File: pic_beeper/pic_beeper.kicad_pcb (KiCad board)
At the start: 2 copper layers, 33 x 26.7 mm, 7 parts, among them J1 Conn_01x06, SW1 SW_SPDT, U1 PIC12F752-IP

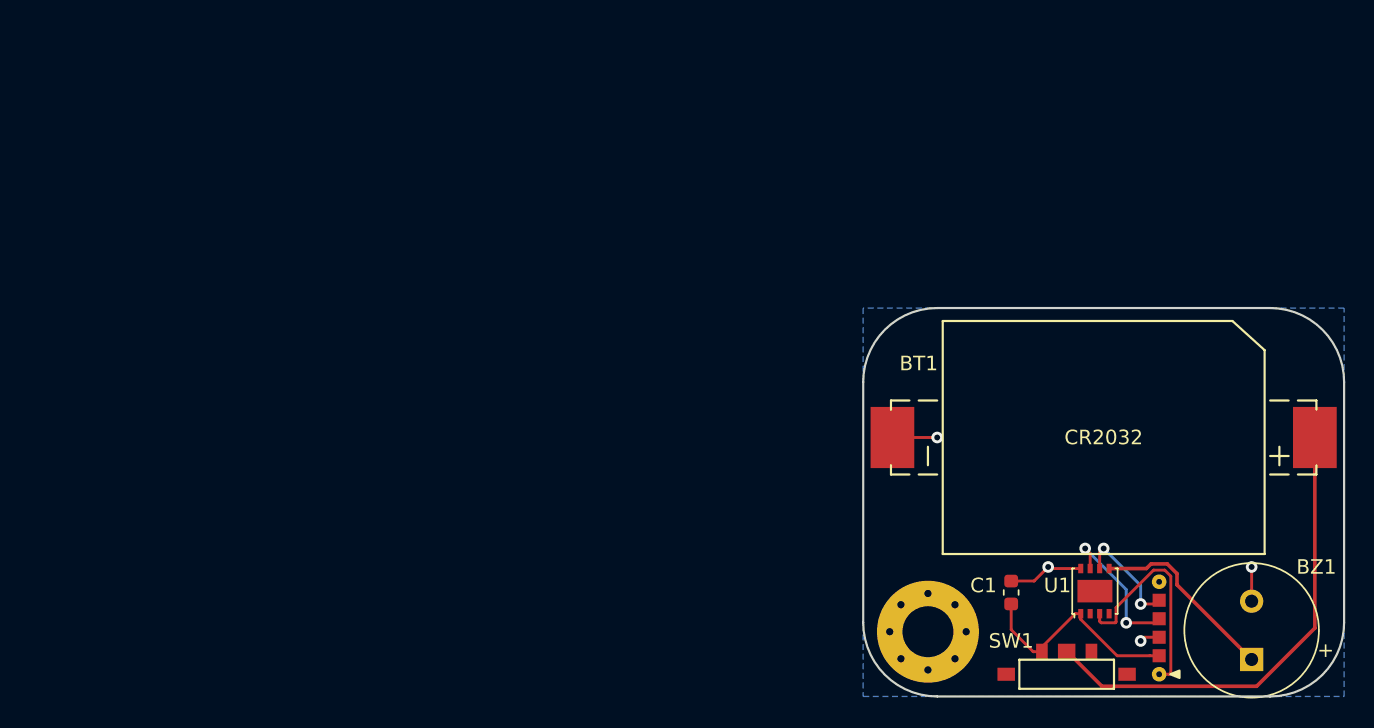
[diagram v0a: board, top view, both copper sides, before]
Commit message: Stop using temp sense osc
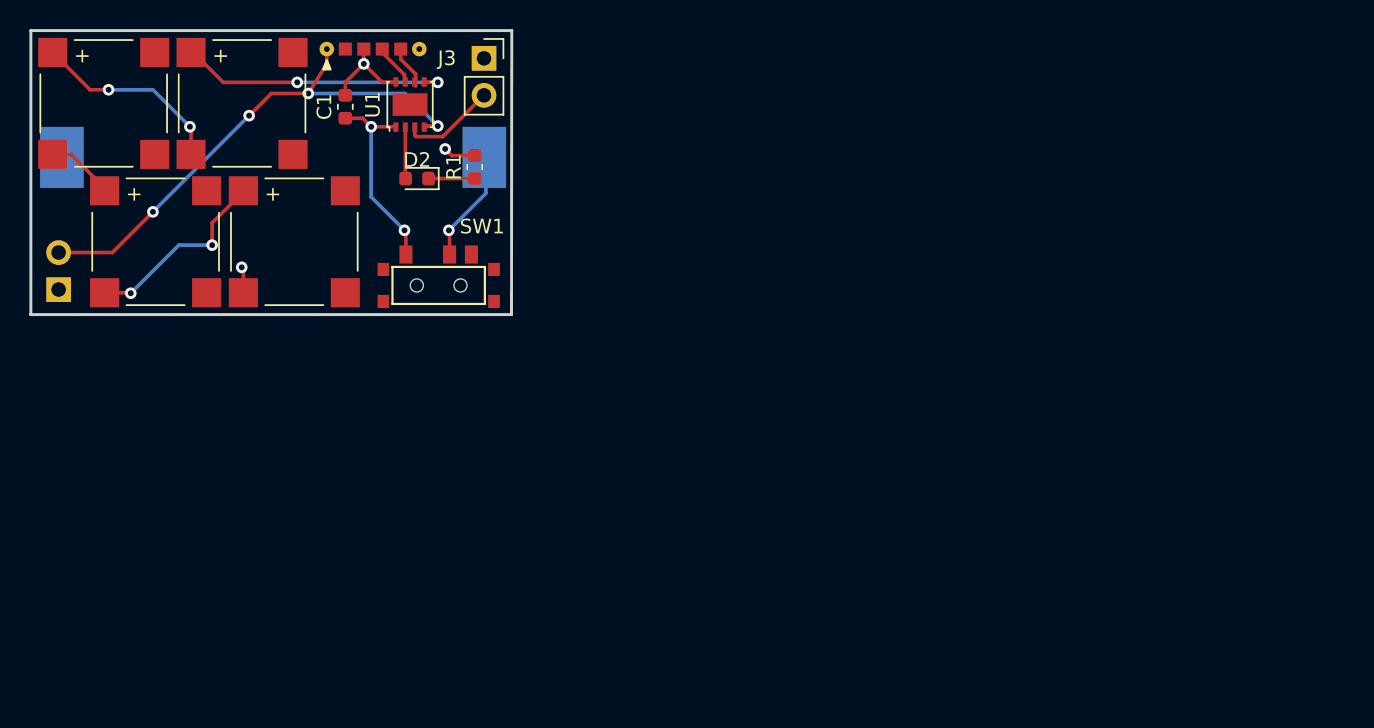
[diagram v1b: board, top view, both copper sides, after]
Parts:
- removed H1: MountingHole_Pad, MountingHole:MountingHole_3.5mm_Pad_Via
- added BZ2: 16R, Buzzer_Beeper:PUIAudio_SMT_0825_S_4_R, F.Cu at (5.00, 5.00)
- added BZ3: 16R, Buzzer_Beeper:PUIAudio_SMT_0825_S_4_R, F.Cu at (8.56, 14.5)
- added BZ4: 16R, Buzzer_Beeper:PUIAudio_SMT_0825_S_4_R, F.Cu at (18.1, 14.5)
- added D2: LED, LED_SMD:LED_0603_1608Metric, F.Cu at (26.5, 10.2)
- added J2: Conn_01x02_Male, Connector_PinHeader_2.54mm:PinHeader_1x02_P2.54mm_Vertical, B.Cu at (1.91, 17.8)
- added J3: Conn_01x02_Female, Connector_PinSocket_2.54mm:PinSocket_1x02_P2.54mm_Vertical, F.Cu at (31.1, 1.91)
- added R1: 140R, Resistor_SMD:R_0603_1608Metric, F.Cu at (30.5, 9.37)
- BT1: moved to B.Cu
- BZ1: value Buzzer -> 16R; footprint Buzzer_Beeper:MagneticBuzzer_CUI_CST-931RP-A -> Buzzer_Beeper:PUIAudio_SMT_0825_S_4_R
- SW1: footprint lib_fp:SW_SPDT_SSAL220100 -> lib_fp:SW_SPDT_SK3296
- U1: value PIC12F752-IP -> PIC12F752
- moved BZ1 79.1 mm to (14.5, 5.00), turned to 0 degrees
- moved J1 66.5 mm to (23.9, 1.27), turned to 0 degrees
- moved BT1 60.2 mm to (16.6, 8.71)
- moved U1 57.7 mm to (26.0, 5.08)
- moved C1 56.6 mm to (21.6, 5.23)
- moved SW1 50.7 mm to (28.0, 17.5), turned to 180 degrees
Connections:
- BZ1 pad 2: -BATT -> Net-(BZ1-Pad2)
- U1 pad 3: /VPP -> /SLAVE_RESET
- U1 pad 4: Net-(U1-Pad4) -> /VPP
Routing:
- net Net-(BT1-Pad1): track 32.8 -> 7.56 mm, vias 0 -> 1
- net /VPP: track 15.2 -> 35.7 mm, vias 0 -> 4
- net Net-(BZ1-Pad2): track 0.00 -> 13.4 mm, vias 0 -> 2
- net Net-(BZ3-Pad2): track 0.00 -> 13.2 mm, vias 0 -> 2
- net /ICSPDAT: track 10.2 -> 2.92 mm, vias 2 -> 0
- net /SLAVE_RESET: track 0.00 -> 6.71 mm
- net /BUZZER: track 13.1 -> 18.5 mm, vias 0 -> 2
- net /ICSPCLK: track 7.73 -> 2.96 mm, vias 2 -> 0
- net Net-(BZ2-Pad2): track 0.00 -> 4.53 mm
- net Net-(D2-Pad2): track 0.00 -> 3.47 mm
- net Net-(D2-Pad1): track 0.00 -> 3.18 mm
- net +BATT: track 15.2 -> 13.3 mm, vias 0 -> 2
- net -BATT: track 12.0 -> 10.4 mm, vias 4 -> 3
- added copper zone on F.Cu, net +BATT
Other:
- board size 33 x 26.7 mm -> 33 x 19.5 mm
- board text added: "v2.1"
- board text removed: "BEEP BEEP awyea"
- board text removed: "PIC Beeper v1.0 John McNelly"

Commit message: Make hardware v2.0
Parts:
- removed BT1: CR2032, lib_fp:BatteryHolder_Q&J-CR2032-BS-6-1
- removed BZ2, BZ3, BZ4: 16R, Buzzer_Beeper:PUIAudio_SMT_0825_S_4_R
- added D1: 40V 5A, Diode_SMD:D_SMA, F.Cu at (20.4, 22.9)
- added G***: LOGO, lib_fp:bird_with_pants_small_flipped, B.Cu at (20.2, 18.4)
- added G***: LOGO, lib_fp:bird_with_pants_small, B.Cu at (24.0, 18.4)
- added J4: Conn_01x03_Female, Connector_PinSocket_2.54mm:PinSocket_1x03_P2.54mm_Vertical, B.Cu at (46.4, 23.5)
- added JP1: Open Jumper, Jumper:SolderJumper-2_P1.3mm_Open_Pad1.0x1.5mm, F.Cu at (32.0, 23.9)
- added Q1: BSS138, Package_TO_SOT_SMD:SOT-23, F.Cu at (26.0, 22.9)
- added R2: 10k, Resistor_SMD:R_0603_1608Metric, F.Cu at (35.6, 13.5)
- added R3: DNP, Resistor_SMD:R_0603_1608Metric, F.Cu at (35.6, 16.7)
- J1: moved to B.Cu
- J2: value Conn_01x02_Male -> JST_PH_01x02_Male_RightAngle; footprint Connector_PinHeader_2.54mm:PinHeader_1x02_P2.54mm_Vertical -> Connector_JST:JST_PH_S2B-PH-K_1x02_P2.00mm_Horizontal; moved to F.Cu
- J3: value Conn_01x02_Female -> Conn_01x03_Male; footprint Connector_PinSocket_2.54mm:PinSocket_1x02_P2.54mm_Vertical -> Connector_PinHeader_2.54mm:PinHeader_1x03_P2.54mm_Vertical
- R1: value 140R -> 680R
- moved J2 40.0 mm to (41.9, 17.8), turned to 180 degrees
- moved J3 20.1 mm to (14.5, 13.2)
- moved C1 16.0 mm to (28.4, 19.7), turned to 0 degrees
- moved SW1 13.3 mm to (39.6, 23.9)
- moved BZ1 13.1 mm to (21.3, 16.2), turned to 90 degrees
- moved J1 12.6 mm to (30.2, 12.2), turned to 180 degrees
- moved U1 11.3 mm to (29.2, 15.9), turned to 270 degrees
- moved R1 6.78 mm to (32.4, 15.9), turned to 270 degrees
- moved D2 3.97 mm to (30.0, 12.1)
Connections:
- BZ1 pad 1: /BUZZER -> +BATT
- J1 pad 6: Net-(J1-Pad6) -> (no net)
- J2 pad 1: -BATT -> /BATT_SWITCH
- J2 pad 2: /VPP -> -BATT
- J3 pad 1: -BATT -> /BATT_SWITCH
- J3 pad 2: /SLAVE_RESET -> /VPP
- SW1 pad 2: Net-(BT1-Pad1) -> /BATT_SWITCH
- SW1 pad 3: Net-(SW1-Pad3) -> (no net)
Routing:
- net /BATT_SWITCH: track 0.00 -> 40.0 mm, vias 0 -> 3
- net /SLAVE_RESET: track 6.71 -> 29.1 mm, vias 0 -> 3
- net Net-(BZ3-Pad2): track 13.2 -> 0.00 mm, vias 2 -> 0
- net /BUZZER: track 18.5 -> 8.69 mm
- net Net-(BT1-Pad1): track 7.56 -> 0.00 mm, vias 1 -> 0
- net +BATT: track 13.3 -> 7.38 mm, vias 2 -> 1
- net Net-(BZ1-Pad2): track 13.4 -> 8.39 mm, vias 2 -> 0
- net /ICSPDAT: track 2.92 -> 7.65 mm, vias 0 -> 1
- net /ICSPCLK: track 2.96 -> 7.54 mm, vias 0 -> 1
- net Net-(BZ2-Pad2): track 4.53 -> 0.00 mm
- net -BATT: track 10.4 -> 6.18 mm, vias 3 -> 5
- net /VPP: track 35.7 -> 37.4 mm, vias 4 -> 5
- net Net-(D2-Pad2): track 3.47 -> 2.39 mm
- net Net-(D2-Pad1): track 3.18 -> 3.69 mm
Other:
- board size 33 x 19.5 mm -> 35.6 x 15.2 mm
- board text added: "Pic Beeper v2.0 For my favorite human."
- board text removed: "v2.1"

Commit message: Dump leftovers
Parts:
- moved G*** 6.39 mm to (17.9, 20.3), turned to 180 degrees
- moved G*** 2.44 mm to (21.7, 20.3), turned to 180 degrees
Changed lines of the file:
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@@
   )
   (setup
-    (last_trace_width 0.8)
+    (last_trace_width 0.25)
     (user_trace_width 0.2)
     (user_trace_width 0.25)
@@
   )
   (module lib_fp:bird_with_pants_small_flipped (layer B.Cu)
-    (at 20.193 18.415)
+    (at 21.717 20.32 180)
     (fp_text reference G*** (at 0 0) (layer B.SilkS) hide
       (effects (font (size 1.524 1.524) (thickness 0.3)) (justify mirror))
@@
   )
   (module lib_fp:bird_with_pants_small (layer B.Cu)
-    (at 24.003 18.415)
+    (at 17.907 20.32 180)
     (fp_text reference G*** (at 0 0) (layer B.SilkS) hide
       (effects (font (size 1.524 1.524) (thickness 0.3)) (justify mirror))
@@
     )
   )
-  (gr_poly (pts (xy 22.098 20.32) (xy 21.59 21.082) (xy 21.59 21.336) (xy 21.717 21.463) (xy 21.971 21.463) (xy 22.098 21.336) (xy 22.098 21.209) (xy 22.098 21.336) (xy 22.225 21.463) (xy 22.352 21.463) (xy 22.479 21.463) (xy 22.606 21.336) (xy 22.606 21.082)) (layer B.SilkS) (width 0.1))
-  (gr_text "Pic Beeper v2.0\nFor my favorite human." (at 13.97 23.495 180) (layer B.SilkS)
-    (effects (font (size 1 1) (thickness 0.15)) (justify left mirror))
+  (gr_poly (pts (xy 19.812 18.415) (xy 20.32 17.653) (xy 20.32 17.399) (xy 20.193 17.272) (xy 19.939 17.272) (xy 19.812 17.399) (xy 19.812 17.526) (xy 19.812 17.399) (xy 19.685 17.272) (xy 19.558 17.272) (xy 19.431 17.272) (xy 19.304 17.399) (xy 19.304 17.653)) (layer B.SilkS) (width 0.1))
+  (gr_text "Pic Beeper v2.0\nFor my favorite human." (at 13.335 24.13) (layer B.SilkS)
+    (effects (font (size 1 1) (thickness 0.15)) (justify right mirror))
   )
   (gr_line (start 12.7 26.035) (end 12.7 10.795) (layer Edge.Cuts) (width 0.15))
@@
     (polygon
       (pts
-        (xy 12.7 10.795) (xy 48.895 10.795) (xy 48.895 26.035) (xy 12.7 26.035)
+        (xy 12.7 10.795) (xy 48.26 10.795) (xy 48.26 26.035) (xy 12.7 26.035)
       )
     )
